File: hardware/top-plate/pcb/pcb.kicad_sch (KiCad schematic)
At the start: 55 parts, among them J1 Conn_01x02, SW1 MT-0-102-A101-M200-RS+PJ

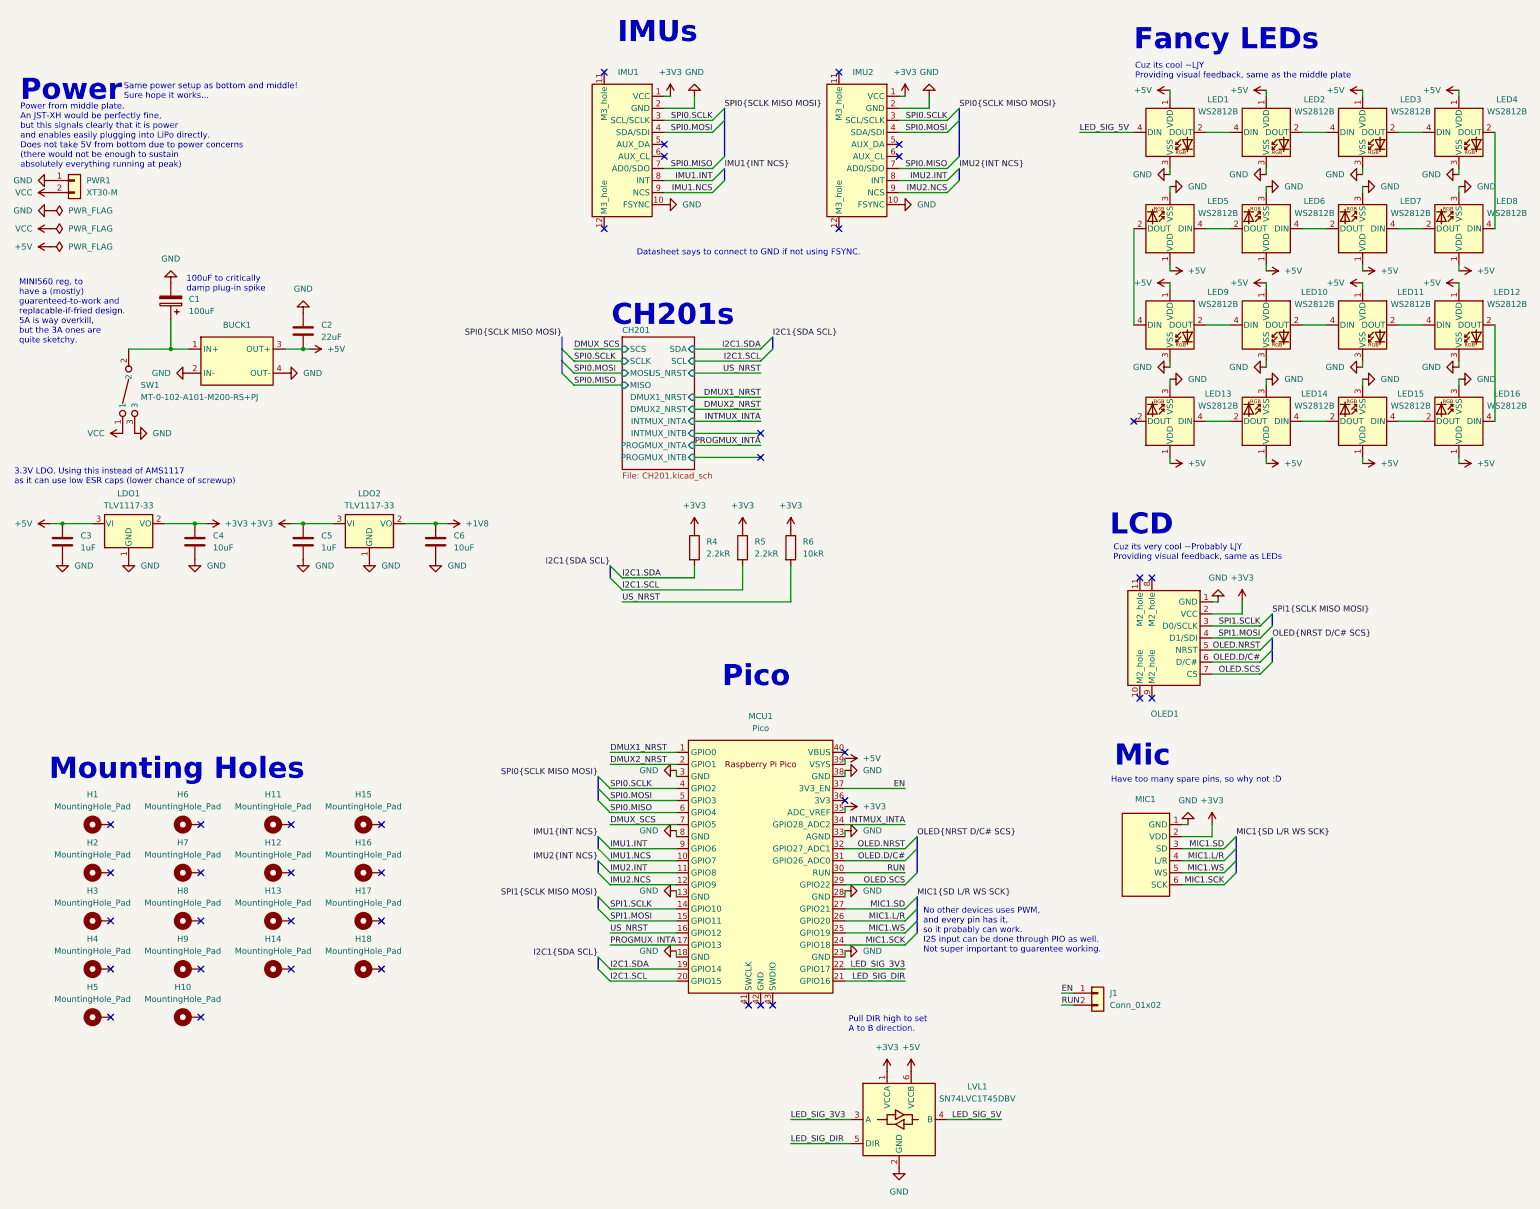
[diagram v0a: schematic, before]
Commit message: some top plate changes
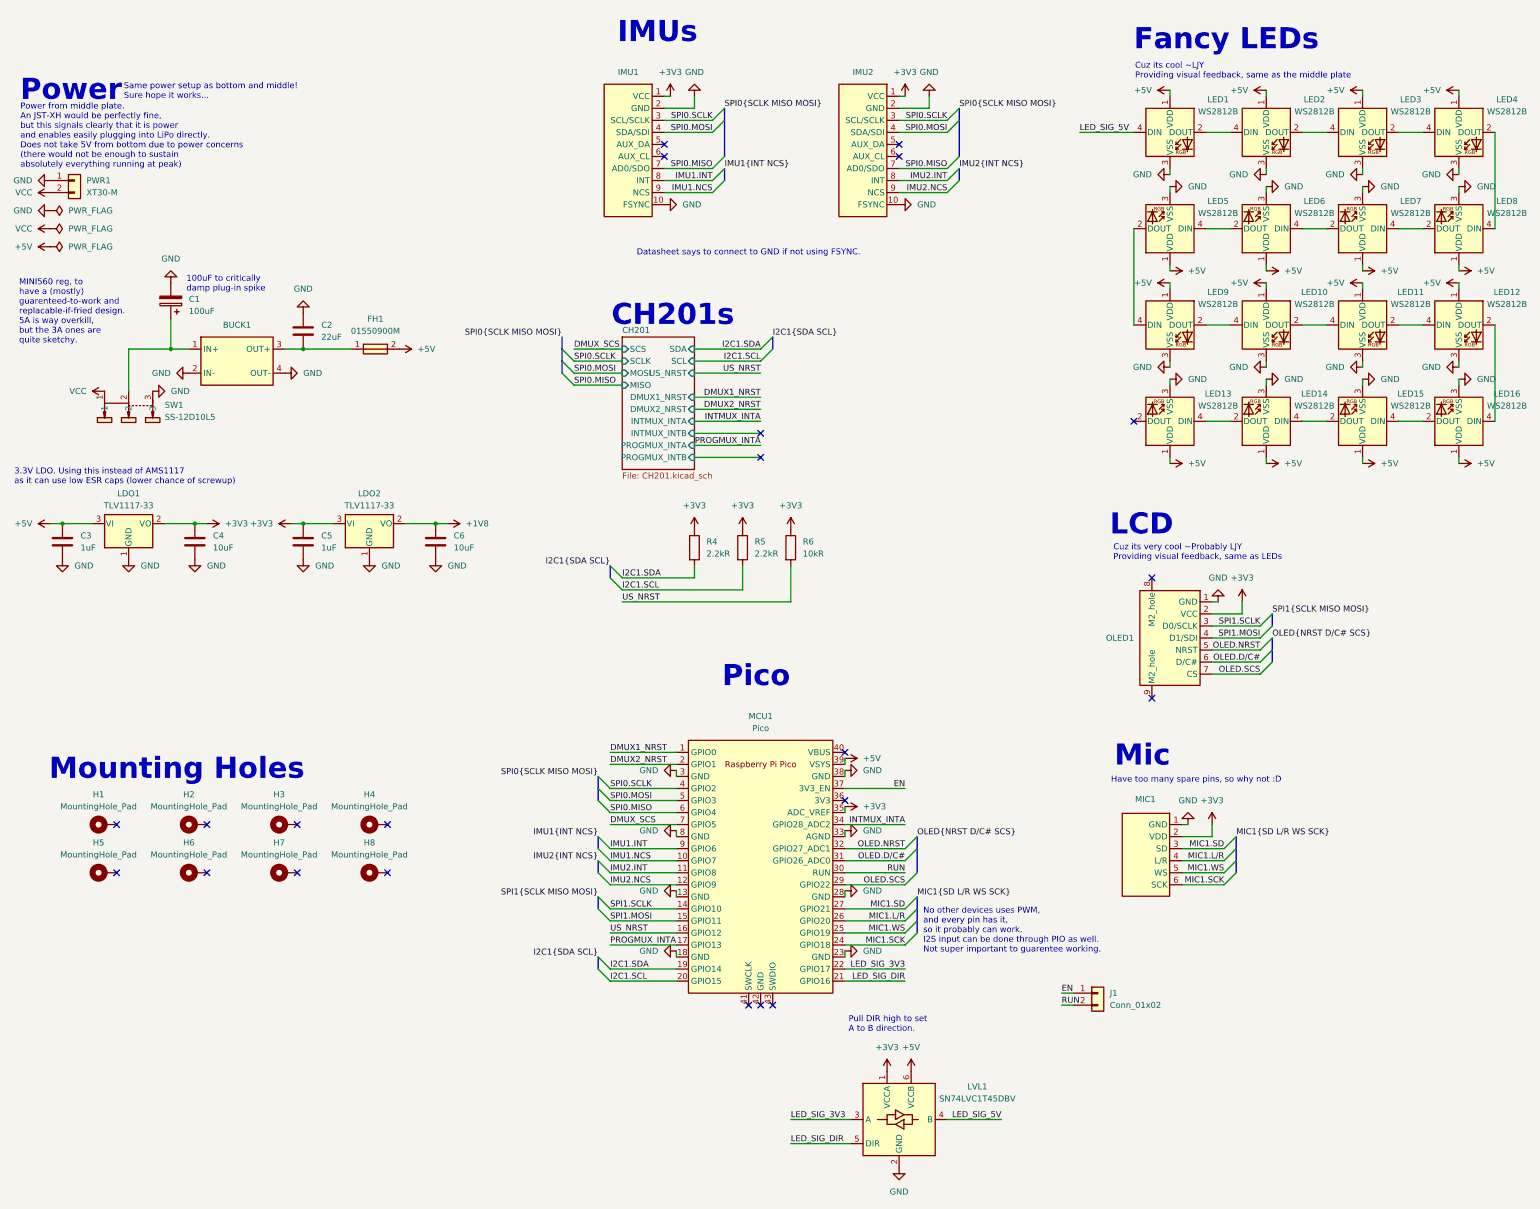
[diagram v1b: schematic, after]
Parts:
- removed H10, H13, H14, H17, H18, H9: MountingHole_Pad, MountingHole:MountingHole_2.2mm_M2_Pad_Via, symbol Mechanical:MountingHole_Pad
- removed H11, H12, H15, H16: MountingHole_Pad, MountingHole:MountingHole_3.2mm_M3_Pad_Via, symbol Mechanical:MountingHole_Pad
- removed IMU1, IMU2: ~, symbol GY-ICM20948V2:GY-ICM20948V2
- removed J1: Conn_01x02, 4ms_Connector:Pins_1x02_2.54mm_TH, symbol PCM_4ms_Connector:Conn_01x02
- removed OLED1: ~, 0.96-inch_OLED_7-pin:0.96-inch_OLED_7-pin, symbol 0.96-inch OLED 7-pin:0.96-inch_OLED_7-pin
- removed SW1: MT-0-102-A101-M200-RS+PJ, EasyEDA:SW-TH_MT-0-103-A101-M200-RS, symbol EasyEDA:MT-0-102-A101-M200-RS+PJ
- added FH1: 01550900M, EasyEDA:FUSE-SMD_L9.8-W5.0, symbol EasyEDA:01550900M
- added IMU1, IMU2: ~, ICM20948:ICM20948-no-mountingholes, symbol GY-ICM20948V2:GY-ICM20948V2-no-mountingholes
- added J1: Conn_01x02, Connector_JST:JST_XH_B2B-XH-A_1x02_P2.50mm_Vertical, symbol Connector_Generic:Conn_01x02
- added OLED1: ~, 0.96-inch_OLED_7-pin:0.96-inch_OLED_7-no-back-mountingholes, symbol 0.96-inch OLED 7-pin:0.96-inch_OLED_7-pin-no-back-mountingholes
- added SW1: SS-12D10L5, EasyEDA:SW-TH_SS-12D10L5, symbol EasyEDA:SS-12D10L5
- C1: footprint Capacitor_SMD:CP_Elec_6.3x7.7 -> Capacitor_SMD:CP_Elec_5x5.7
- C2, C3, C4, C5, C6: footprint PCM_Capacitor_SMD_AKL:C_1206_3216Metric_Pad1.33x1.80mm_HandSolder -> PCM_Capacitor_SMD_AKL:C_0805_2012Metric_Pad1.15x1.40mm_HandSolder
- H1, H2, H3, H6, H7, H8: footprint MountingHole:MountingHole_3.2mm_M3_Pad_Via -> MountingHole:MountingHole_2.2mm_M2_Pad_Via
- MCU1: footprint RP-Pico Libraries:RPi_Pico_SMD_TH -> RP-Pico Libraries:RPi_Pico_SMD_TH_USBC_cable_cutout
- MIC1: footprint (none) -> INMP441:INMP441
- R4, R5, R6: footprint PCM_Resistor_SMD_AKL:R_1206_3216Metric_Pad1.30x1.75mm_HandSolder -> PCM_Resistor_SMD_AKL:R_0805_2012Metric_Pad1.15x1.40mm_HandSolder
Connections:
- net +3V3: now also IMU1.1 (VCC), IMU2.1 (VCC), OLED1.2 (VCC)
- net +5V: now also FH1.2; no longer BUCK1.3 (OUT+), C2.2
- net EN: now also J1.1 (Pin_1)
- net GND: now also IMU1.10 (FSYNC), IMU1.2 (GND), IMU2.10 (FSYNC), IMU2.2 (GND), OLED1.1 (GND), SW1.3
- net IMU1.INT: now also IMU1.8 (INT)
- net IMU1.NCS: now also IMU1.9 (NCS)
- net IMU2.INT: now also IMU2.8 (INT)
- net IMU2.NCS: now also IMU2.9 (NCS)
- net OLED.D/C#: now also OLED1.6 (D/C#)
- net OLED.NRST: now also OLED1.5 (NRST)
- net OLED.SCS: now also OLED1.7 (CS)
- net RUN: now also J1.2 (Pin_2)
- net SPI0.MISO: now also IMU1.7 (AD0/SDO), IMU2.7 (AD0/SDO)
- net SPI0.MOSI: now also IMU1.4 (SDA/SDI), IMU2.4 (SDA/SDI)
- net SPI0.SCLK: now also IMU1.3 (SCL/SCLK), IMU2.3 (SCL/SCLK)
- net SPI1.MOSI: now also OLED1.4 (D1/SDI)
- net SPI1.SCLK: now also OLED1.3 (D0/SCLK)
- net VCC: now also SW1.1
- net at BUCK1.1 (IN+), C1.1: now also SW1.2
- new net: BUCK1.3 (OUT+), C2.2, FH1.1
- no-connect marks 38 -> 22

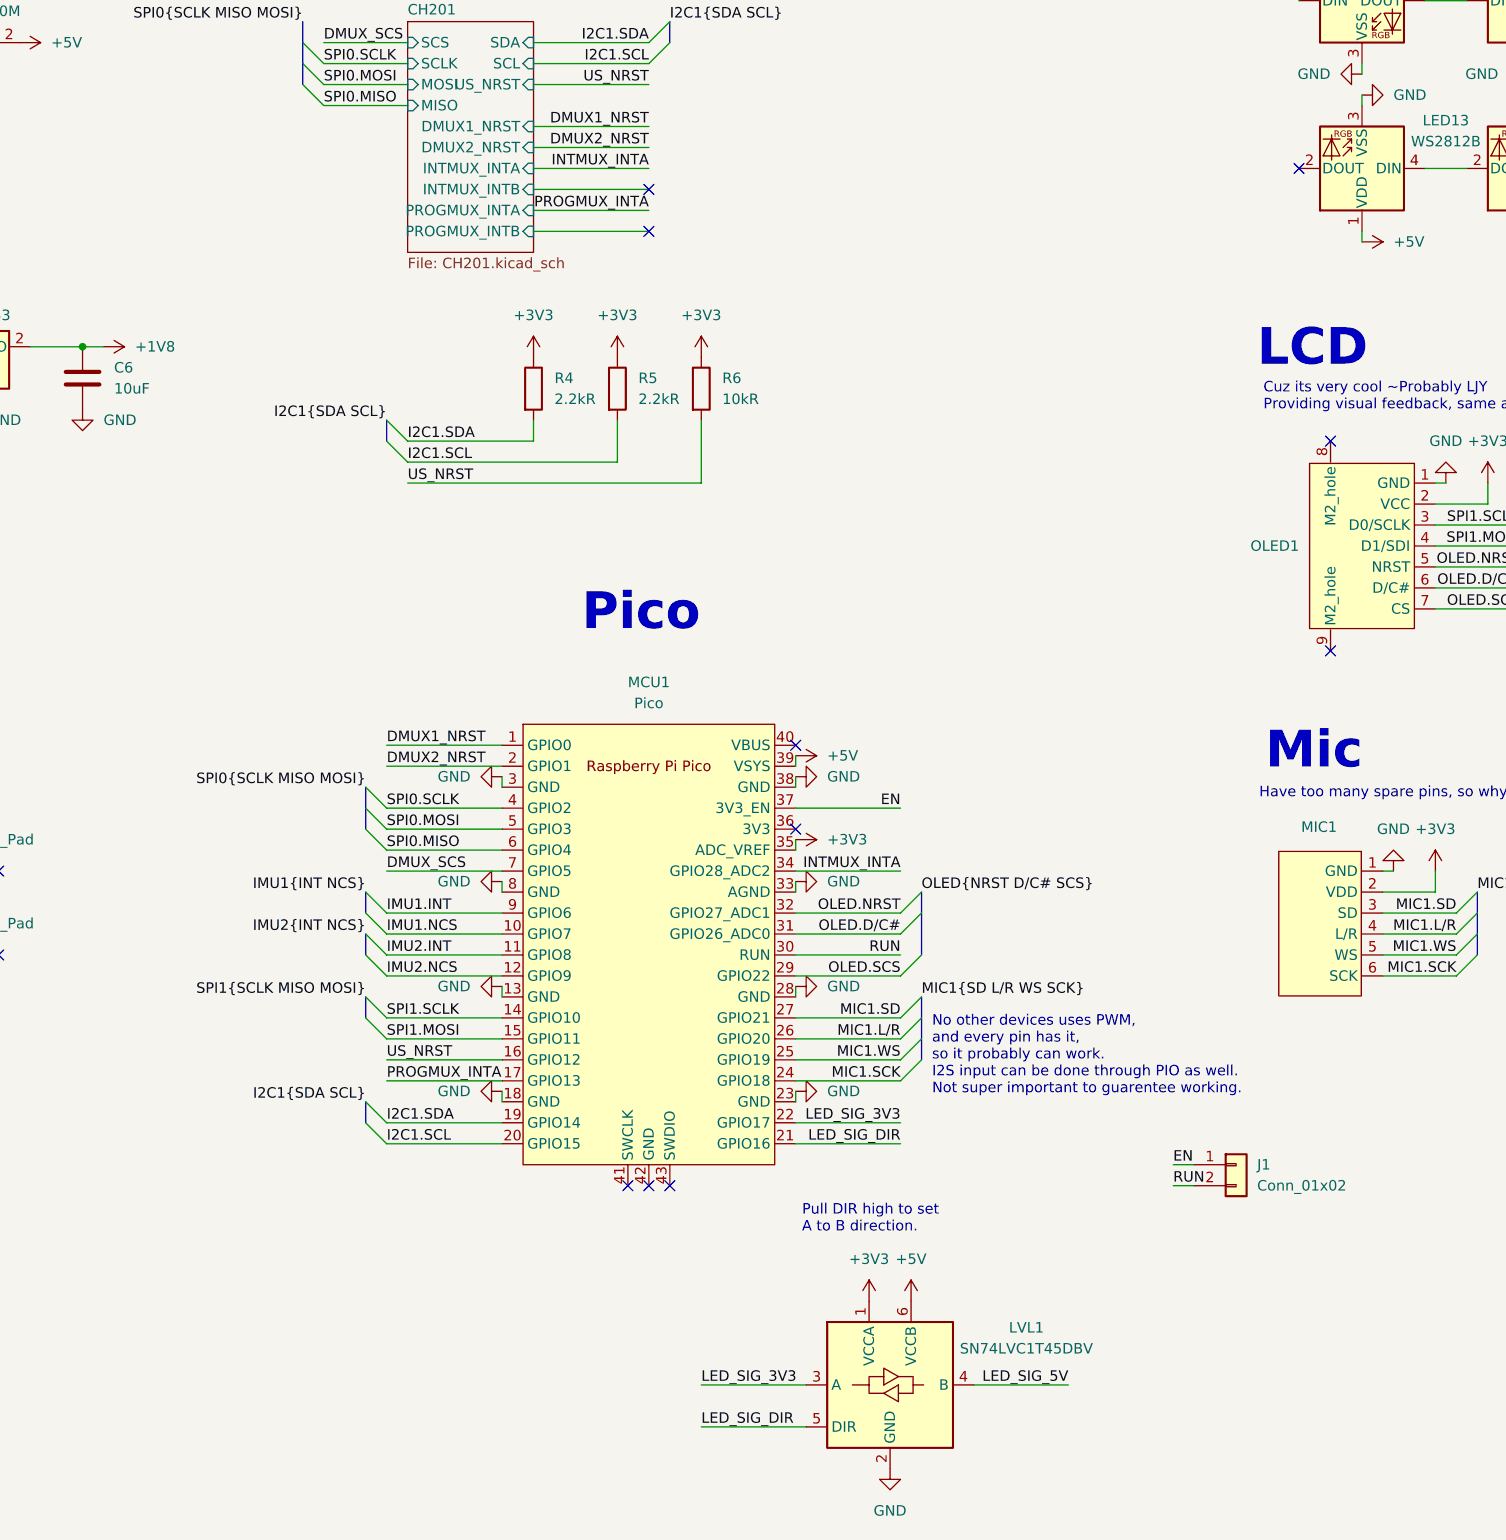
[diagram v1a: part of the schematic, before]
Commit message: fixed up bottom plate schematic. do not run a global symbol update! all modified symbols as of now are intentionally modified locally.
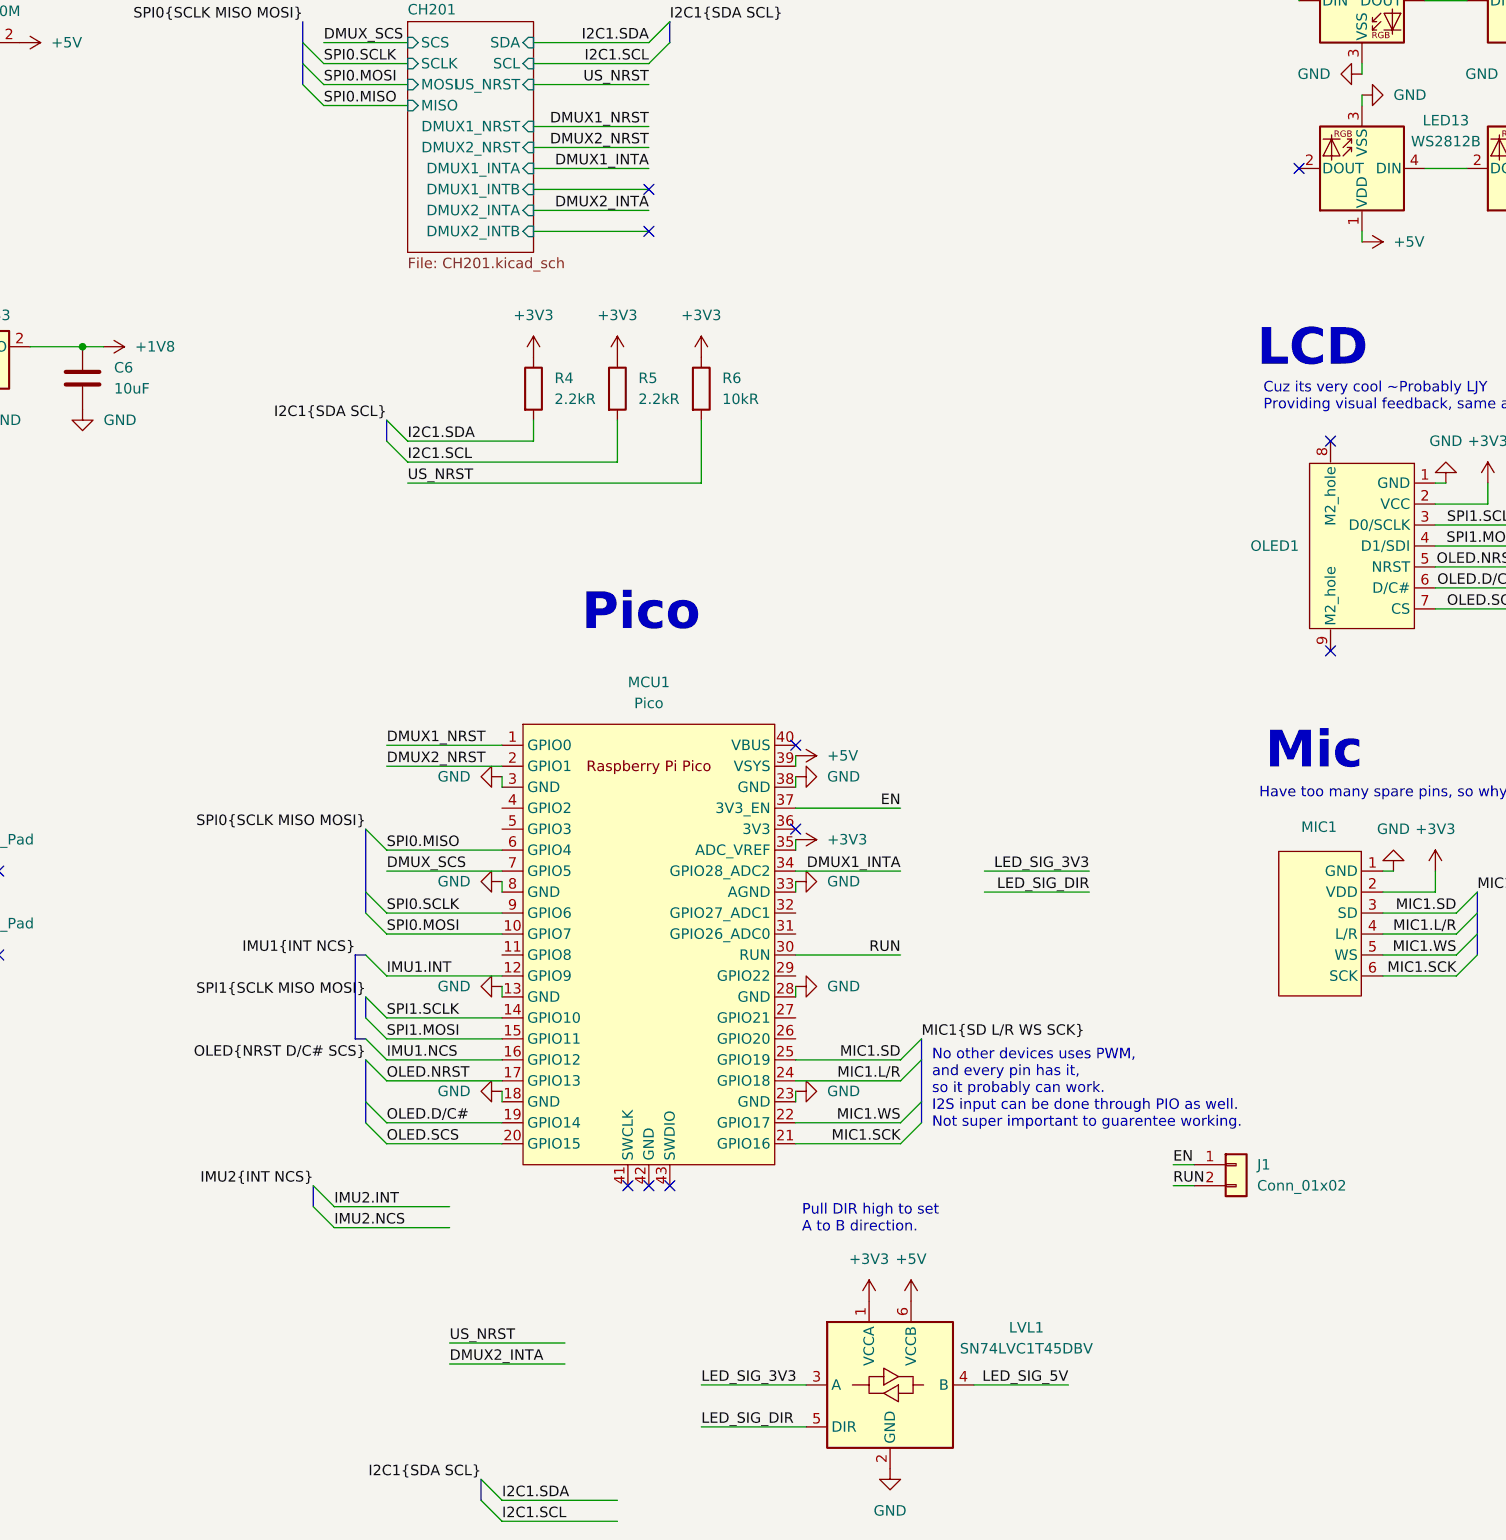
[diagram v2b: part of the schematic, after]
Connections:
- net PROGMUX_INTA is gone; now on net OLED.NRST: MCU1.17 (GPIO13)
- net I2C1.SCL: no longer MCU1.20 (GPIO15)
- net I2C1.SDA: no longer MCU1.19 (GPIO14)
- net IMU1.INT: now also MCU1.12 (GPIO9); no longer MCU1.9 (GPIO6)
- net IMU1.NCS: now also MCU1.16 (GPIO12); no longer MCU1.10 (GPIO7)
- net IMU2.INT: no longer MCU1.11 (GPIO8)
- net IMU2.NCS: no longer MCU1.12 (GPIO9)
- net LED_SIG_3V3: no longer MCU1.22 (GPIO17)
- net LED_SIG_DIR: no longer MCU1.21 (GPIO16)
- net MIC1.L/R: now also MCU1.24 (GPIO18); no longer MCU1.26 (GPIO20)
- net MIC1.SCK: now also MCU1.21 (GPIO16); no longer MCU1.24 (GPIO18)
- net MIC1.SD: now also MCU1.25 (GPIO19); no longer MCU1.27 (GPIO21)
- net MIC1.WS: now also MCU1.22 (GPIO17); no longer MCU1.25 (GPIO19)
- net OLED.D/C#: now also MCU1.19 (GPIO14); no longer MCU1.31 (GPIO26_ADC0)
- net OLED.NRST: no longer MCU1.32 (GPIO27_ADC1)
- net OLED.SCS: now also MCU1.20 (GPIO15); no longer MCU1.29 (GPIO22)
- net SPI0.MOSI: now also MCU1.10 (GPIO7); no longer MCU1.5 (GPIO3)
- net SPI0.SCLK: now also MCU1.9 (GPIO6); no longer MCU1.4 (GPIO2)
- net US_NRST: no longer MCU1.16 (GPIO12)
- net INTMUX_INTA renamed DMUX1_INTA
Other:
- sheet CH201 ports: added DMUX1_INTA, DMUX1_INTB, DMUX2_INTA, DMUX2_INTB; removed INTMUX_INTA, INTMUX_INTB, PROGMUX_INTA, PROGMUX_INTB
